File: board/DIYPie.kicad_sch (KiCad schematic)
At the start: 7 parts

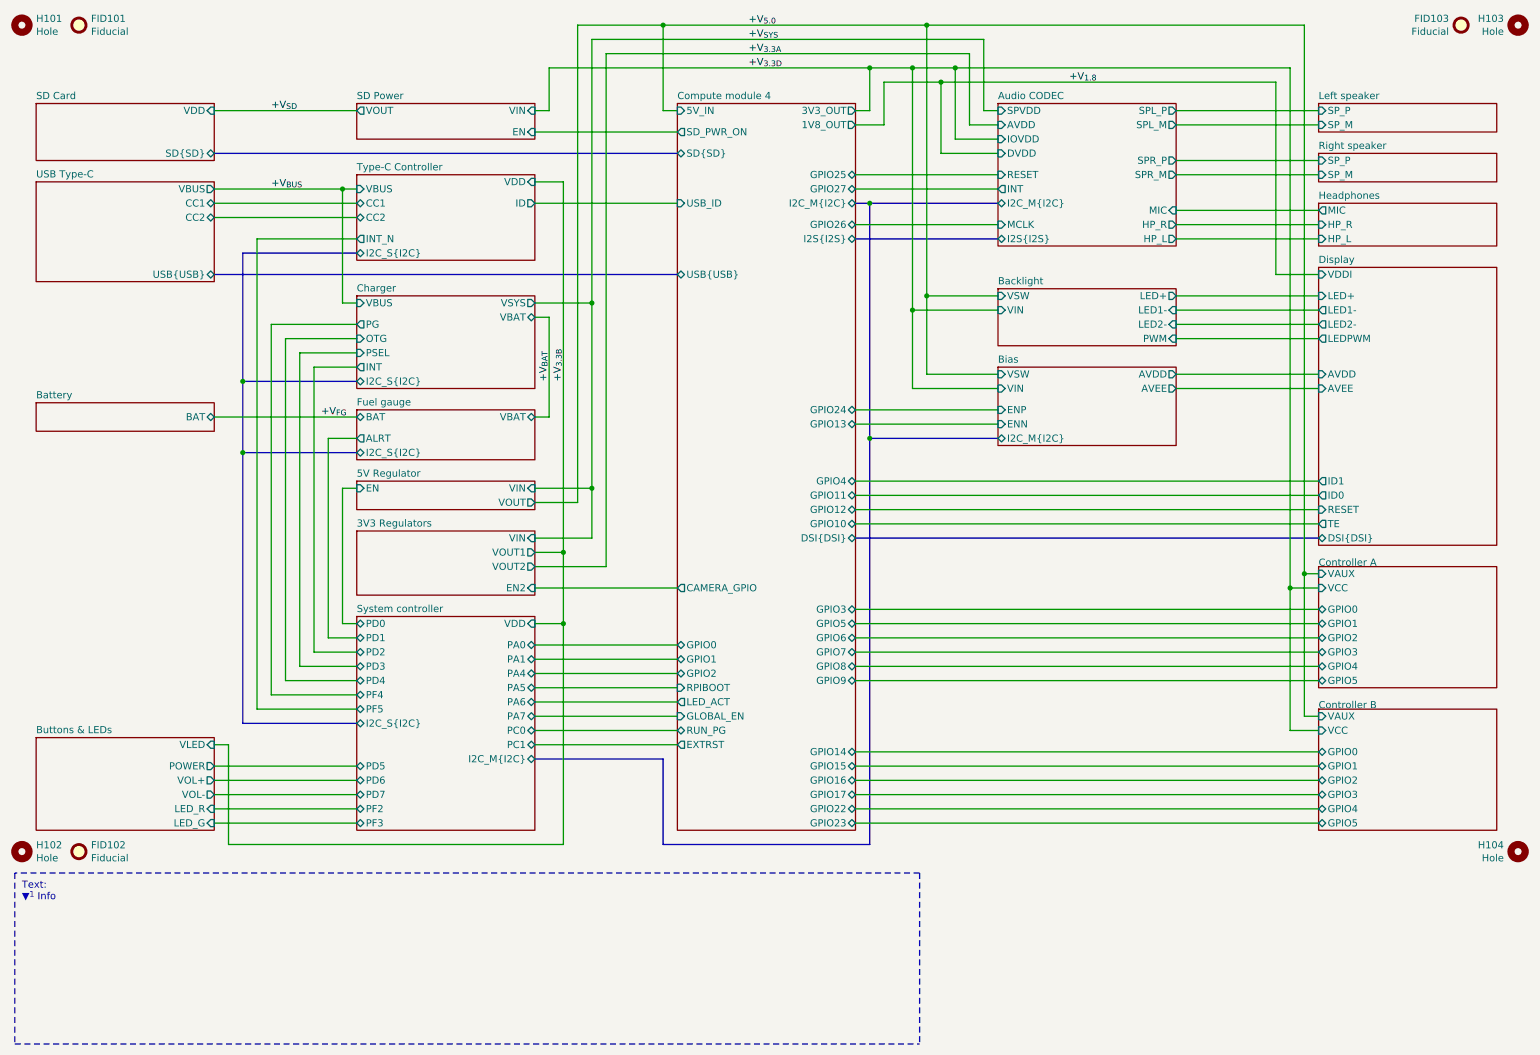
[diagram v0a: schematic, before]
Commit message: Added testpoints and other fixes
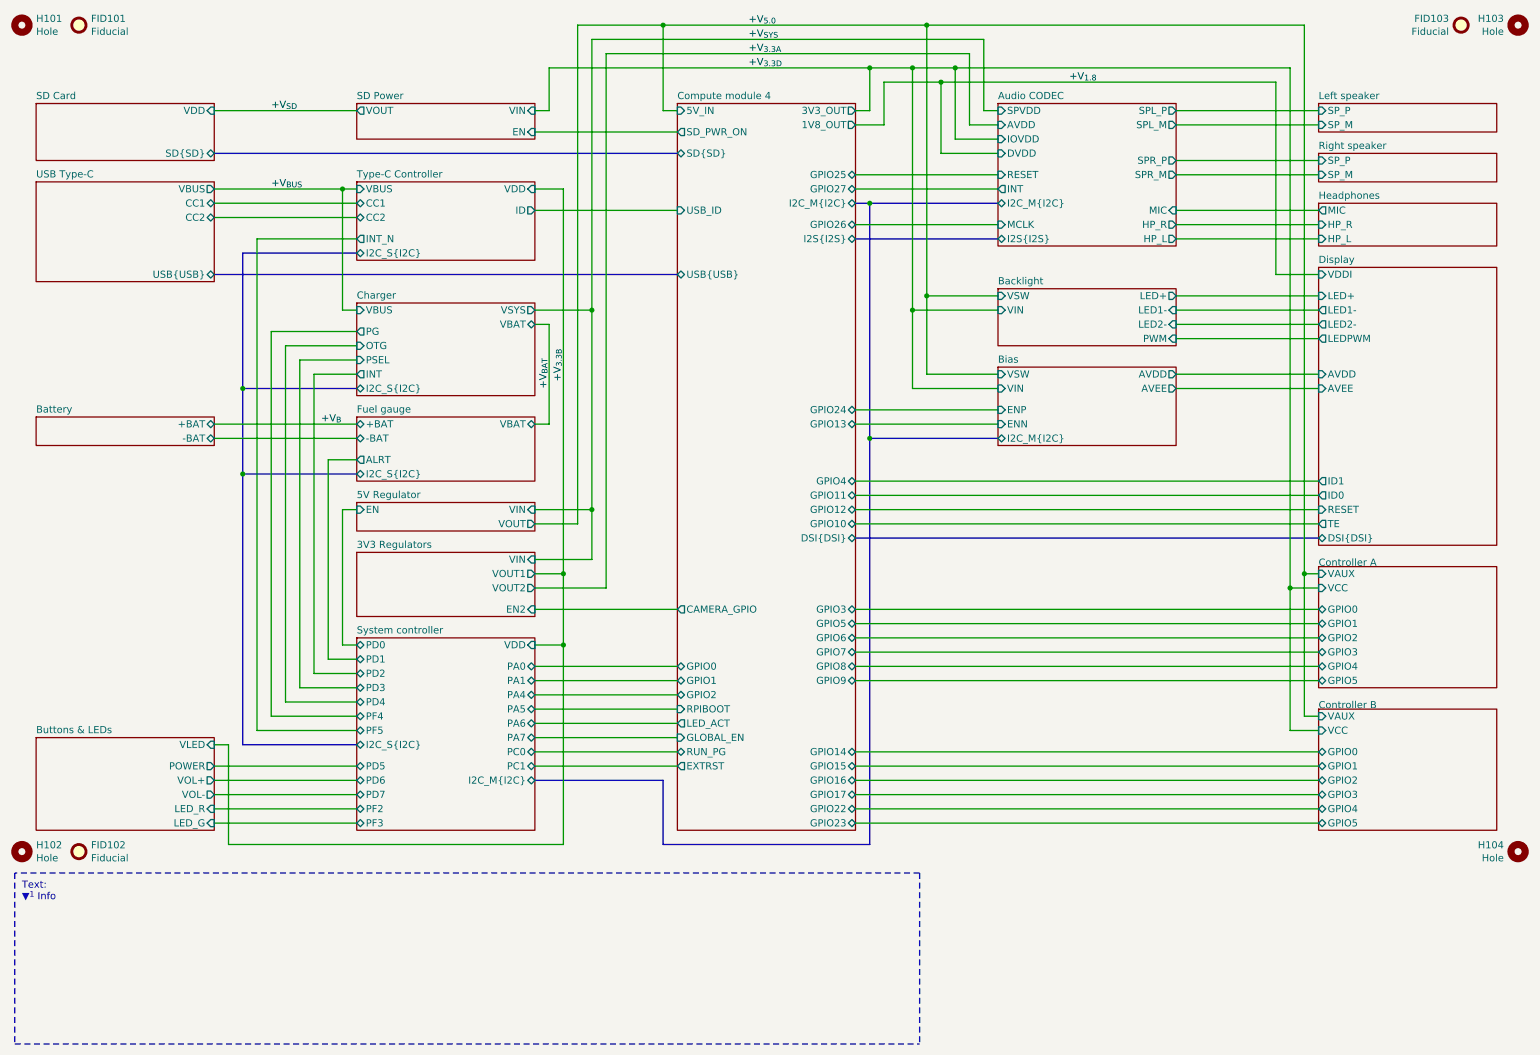
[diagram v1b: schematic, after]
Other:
- sheet Battery ports: added +BAT, -BAT; removed BAT
- sheet Fuel gauge ports: added +BAT, -BAT; removed BAT
